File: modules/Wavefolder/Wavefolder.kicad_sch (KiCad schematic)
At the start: 16 parts, among them J10 Conn_Front, J104 WQP-PJ398, J105 WQP-PJ398, J106 WQP-PJ398, J107 WQP-PJ398, J11 Conn_Back, J9 Conn_Eurorack_10, U3 TL072

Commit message: Munger re-design - schematic done, PCB started
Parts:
- added C1, C2: 680N, -lmp-misc:C_Rect_L7.2mm_W4.5mm_P5.00mm, symbol -lmp:CF
- added C3, C4: 10U, -lmp-misc:C_Radial_D5.0mm_H5.0mm_P2.50mm, symbol -lmp-synth:CNP_10U
- added C3, C4: 100N, -lmp-misc:C_Disc_D5.0mm_W2.5mm_P2.50mm, symbol -lmp:CC_100N
- added Q1, Q4, Q6, Q8: 2N3904, -lmp-misc:TO-92_Inline_Wide, symbol -lmp:Q_NPN_2N3904
- added Q2, Q3, Q5, Q7: 2N3906, -lmp-misc:TO-92_Inline_Wide, symbol -lmp:Q_PNP_2N3906
- added R10, R11, R19, R20, R25, R26, R4, R5: 15K, -lmp-misc:R_Axial_DIN0207_L6.3mm_D2.5mm_P7.62mm_Horizontal, symbol -lmp:R_1%_0W166
- added R12, R21, R27, R6: 10K, -lmp-misc:R_Axial_DIN0207_L6.3mm_D2.5mm_P7.62mm_Horizontal, symbol -lmp:R_1%_0W166
- added R13, R28: 200K, -lmp-misc:R_Axial_DIN0207_L6.3mm_D2.5mm_P7.62mm_Horizontal, symbol -lmp:R_1%_0W166
- added R14, R29: 1K, -lmp-misc:R_Axial_DIN0207_L6.3mm_D2.5mm_P10.16mm_Horizontal, symbol -lmp-synth:R_1K_Output
- added R15, R17, R2, R30: 100K, -lmp-misc:R_Axial_DIN0207_L6.3mm_D2.5mm_P7.62mm_Horizontal, symbol -lmp:R_1%_0W166
- added R16: 499K, -lmp-misc:R_Axial_DIN0207_L6.3mm_D2.5mm_P7.62mm_Horizontal, symbol -lmp:R_1%_0W166
- added R18, R3: 18K, -lmp-misc:R_Axial_DIN0207_L6.3mm_D2.5mm_P7.62mm_Horizontal, symbol -lmp:R_1%_0W166
- added R22, R7: 120K, -lmp-misc:R_Axial_DIN0207_L6.3mm_D2.5mm_P7.62mm_Horizontal, symbol -lmp:R_1%_0W166
- added R23, R8: 27K, -lmp-misc:R_Axial_DIN0207_L6.3mm_D2.5mm_P7.62mm_Horizontal, symbol -lmp:R_1%_0W166
- added R24, R9: 68K, -lmp-misc:R_Axial_DIN0207_L6.3mm_D2.5mm_P7.62mm_Horizontal, symbol -lmp:R_1%_0W166
- added U1: TL074, Package_DIP:DIP-14_W7.62mm, symbol -lmp-opamp:TL074
- added U2: TL072, Package_DIP:DIP-8_W7.62mm, symbol -lmp-opamp:TL072
- J10: footprint Connector_PinSocket_2.54mm:PinSocket_1x18_P2.54mm_Vertical -> Connector_PinSocket_2.54mm:PinSocket_1x09_P2.54mm_Vertical; symbol Connector_Generic:Conn_01x18 -> Connector_Generic:Conn_01x09
- J11: footprint Connector_PinHeader_2.54mm:PinHeader_1x18_P2.54mm_Horizontal -> Connector_PinHeader_2.54mm:PinHeader_1x09_P2.54mm_Horizontal; symbol Connector_Generic:Conn_01x18 -> Connector_Generic:Conn_01x09
- renumbered J104 to J1, J106 to J2, J105 to J3, J107 to J4, RV101 to RV1, RV102 to RV2
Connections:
- net +12V: now also C3.1, R10.1, R19.1, R25.1, R4.1, U1.4 (V+); no longer J10.17 (Pin_17), J11.17 (Pin_17)
- net -12V: now also C4.2, R11.2, R20.2, R26.2, R5.2, U1.11 (V-)
- net GND: now also J10.1 (Pin_1), J10.3 (Pin_3), J10.5 (Pin_5), J10.7 (Pin_7), J10.9 (Pin_9), J11.1 (Pin_1), J11.3 (Pin_3), J11.5 (Pin_5), J11.7 (Pin_7), J11.9 (Pin_9), J2.S, J3.S, J4.S, RV2.1, C3.2, C4.1, R15.2, R17.2, R2.2, R24.2, R30.2, R9.2, U1.12 (+), U1.3 (+), U2.3 (+), U2.5 (+); no longer J10.18 (Pin_18), J11.18 (Pin_18)
- net IN-ATTEN-1: now also J10.2 (Pin_2), J11.2 (Pin_2), U1.5 (+)
- net IN-ATTEN-2: now reaches J10.4 (Pin_4), J11.4 (Pin_4)
- net IN-ATTEN-2: now also RV2.2, U1.10 (+)
- net OUT-1: now reaches J10.6 (Pin_6), J11.6 (Pin_6)
- net OUT-1: now also J2.T, J3.TN, C3.2, R15.1
- net OUT-2: now reaches J10.8 (Pin_8), J11.8 (Pin_8)
- net OUT-2: now also J4.T, C4.2, R30.1
- net at RV2.3: now also R16.2
- net at J3.T: now also R16.1
- new net: Q6.1 (E), R20.1
- new net: C2.1, R22.2, U1.14
- new net: C2.2, R23.1
- new net: R13.2, R14.1, U2.1
- new net: R12.2, R13.1, U2.2 (-)
- new net: Q7.1 (E), R25.2
- new net: Q7.2 (B), Q8.2 (B), R23.2, R24.1
- new net: Q7.3 (C), Q8.3 (C), R27.1
- new net: Q5.2 (B), Q6.2 (B), R18.2, U1.8
- new net: R17.1, R18.1, U1.9 (-)
- new net: Q4.1 (E), R11.1
- new net: Q3.2 (B), Q4.2 (B), R8.2, R9.1
- new net: R2.1, R3.1, U1.6 (-)
- new net: Q1.2 (B), Q2.2 (B), R3.2, U1.7
- new net: C4.1, R29.2
- new net: Q3.1 (E), R10.2
- new net: R21.2, R22.1, U1.13 (-)
- new net: Q5.3 (C), Q6.3 (C), R21.1
- new net: Q2.1 (E), R4.2
- new net: C1.1, R7.2, U1.1
- new net: C1.2, R8.1
- new net: Q1.3 (C), Q2.3 (C), R6.1
- new net: R6.2, R7.1, U1.2 (-)
- new net: Q8.1 (E), R26.1
- new net: Q1.1 (E), R5.1
- new net: Q5.1 (E), R19.2
- new net: R27.2, R28.1, U2.6 (-)
- new net: C3.1, R14.2
- new net: Q3.3 (C), Q4.3 (C), R12.1
- new net: R28.2, R29.1, U2.7
- no-connect marks 0 -> 2
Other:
- note added: "Channel 2"
- note added: "TODO: fields for C1, C2"
- note removed: "TODO: normal this from OUT1"
- moved on the sheet: J1, J2, J3, J4, R1, RV1, RV2, U3C

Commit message: Munger re-design - PCB wip
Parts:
- renumbered Q2 to Q1, Q1 to Q2
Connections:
- net GND: now also U2.3 (+), U2.5 (+); no longer U2.3 (+), U2.5 (+)
- net at R13.2, R14.1: now also U2.7; no longer U2.1
- net at R12.2, R13.1: now also U2.6 (-); no longer U2.2 (-)
- net at R27.2, R28.1: now also U2.2 (-); no longer U2.6 (-)
- net at R28.2, R29.1: now also U2.1; no longer U2.7

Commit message: Munger re-design - PCB wip
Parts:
- R20: footprint -lmp-misc:R_Axial_DIN0207_L6.3mm_D2.5mm_P7.62mm_Horizontal -> -lmp-stripboard:SB_Gen_1

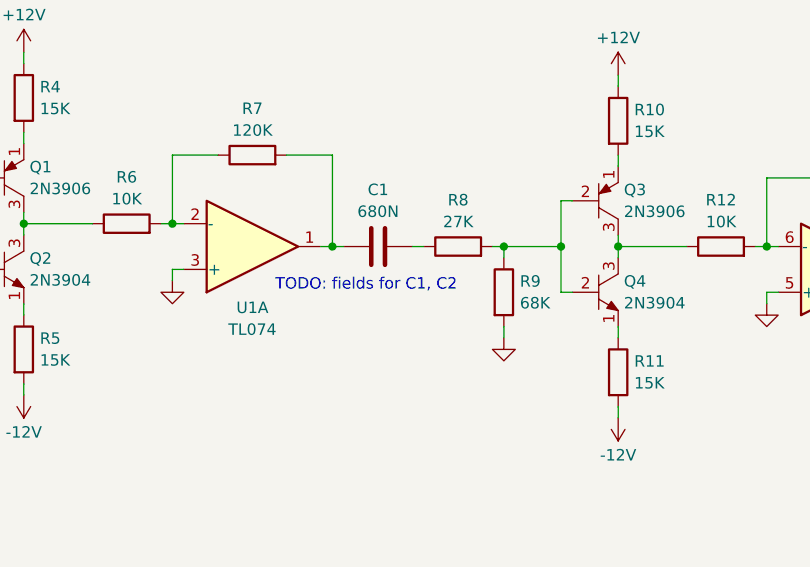
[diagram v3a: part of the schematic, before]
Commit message: Munger re-design - PCB layout mostly done
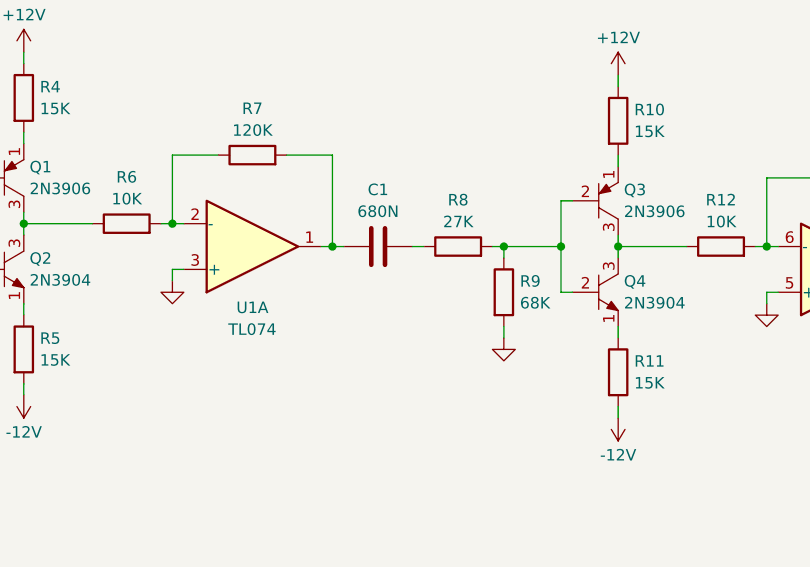
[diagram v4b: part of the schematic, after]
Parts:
- C1, C2: Distributor (none) -> Mouser; DistributorPartLink (none) -> https://www.mouser.ca/ProductDetail/?qs=Jv4FAWB%252B0HZwVuY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; DistributorPartNum (none) -> 80-R82DC3680AA60K; Manufacturer (none) -> KEMET; ManufacturerPartNum (none) -> R82DC3680AA60K
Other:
- note removed: "TODO: fields for C1, C2"

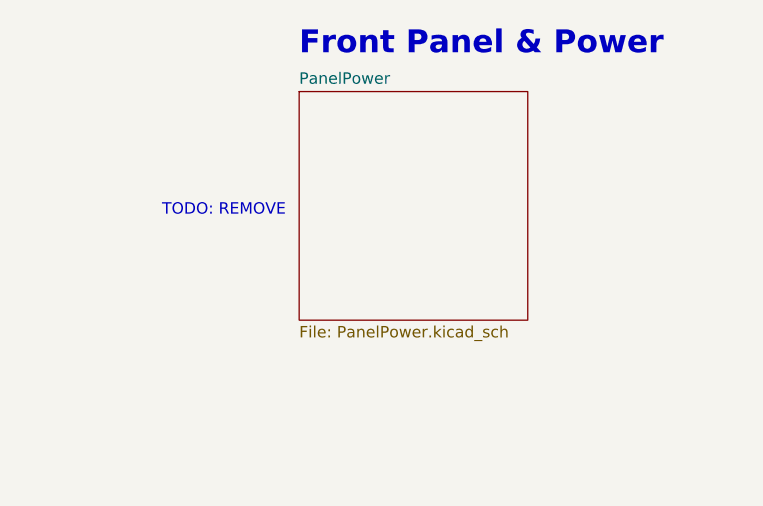
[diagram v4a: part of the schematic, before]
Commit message: Munger re-design - remove unused schematic sheet
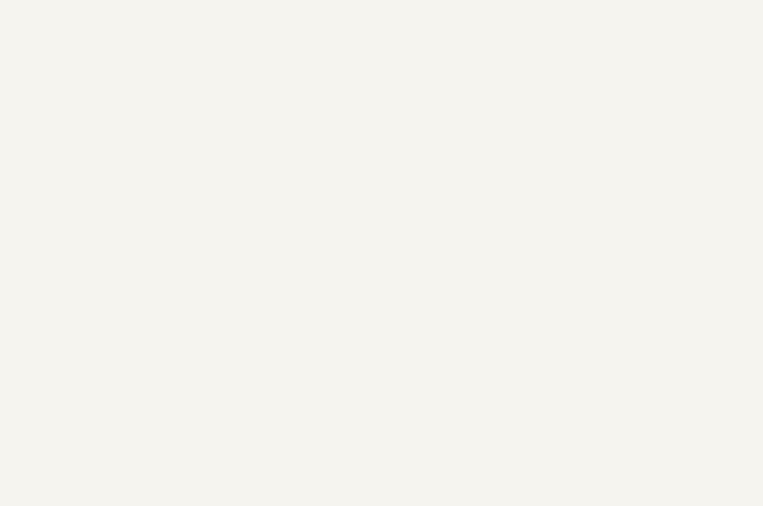
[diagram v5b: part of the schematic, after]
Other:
- removed sheet PanelPower
- note removed: "Front Panel & Power"
- note removed: "TODO: REMOVE"

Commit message: Munger re-design - BOM - wip
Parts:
- C101: renamed from C2; value 10U -> CP_10U
- C102: renamed from C1; value 10U -> CP_10U
- renumbered C3 to C103, C4 to C104, C3 to C105, C4 to C106, J9 to J101, J10 to J102, J11 to J103, U3 to U2

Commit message: Munger re-design - BOM - wip
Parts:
- C101, C102: value CP_10U -> 10U; Value2 35 VDC -> (none)
- R1, R16: DistributorPartLink https://www.mouser.ca/c/?m=YAGEO&power+rating=166+mW+(1%2f6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 -> https://www.mouser.ca/ProductDetail/YAGEO/MFR-25FTE52-499K?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; DistributorPartNum 603-MFR-12* -> 603-MFR-25FTE52-499K; ManufacturerPartNum MFR-12* -> MFR-25FTE52-499K; Value2 1%, 1/6 W -> 1%, 1/4 W
- R10, R11, R19, R20, R25, R26, R4, R5: DistributorPartLink https://www.mouser.ca/c/?m=YAGEO&power+rating=166+mW+(1%2f6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 -> https://www.mouser.ca/ProductDetail/YAGEO/MFR-12FTF52-15K?q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; DistributorPartNum 603-MFR-12* -> 603-MFR-12FTF52-15K; ManufacturerPartNum MFR-12* -> MFR-12FTF52-15K
- R12, R21, R27, R6: DistributorPartLink https://www.mouser.ca/c/?m=YAGEO&power+rating=166+mW+(1%2f6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 -> https://www.mouser.ca/ProductDetail/YAGEO/MFR-12FTF52-10K?q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; DistributorPartNum 603-MFR-12* -> 603-MFR-12FTF52-10K; ManufacturerPartNum MFR-12* -> MFR-12FTF52-10K
- R13, R28: DistributorPartLink https://www.mouser.ca/c/?m=YAGEO&power+rating=166+mW+(1%2f6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 -> https://www.mouser.ca/ProductDetail/YAGEO/MFR-12FTF52-200K?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; DistributorPartNum 603-MFR-12* -> 603-MFR-12FTF52-200K; ManufacturerPartNum MFR-12* -> MFR-12FTF52-200K
- R15, R17, R2, R30: DistributorPartLink https://www.mouser.ca/c/?m=YAGEO&power+rating=166+mW+(1%2f6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 -> https://www.mouser.ca/ProductDetail/YAGEO/MFR-12FTF52-100K?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; DistributorPartNum 603-MFR-12* -> 603-MFR-12FTF52-100K; ManufacturerPartNum MFR-12* -> MFR-12FTF52-100K
- R18, R3: DistributorPartLink https://www.mouser.ca/c/?m=YAGEO&power+rating=166+mW+(1%2f6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 -> https://www.mouser.ca/ProductDetail/YAGEO/MFR-12FTF52-18K?q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; DistributorPartNum 603-MFR-12* -> 603-MFR-12FTF52-18K; ManufacturerPartNum MFR-12* -> MFR-12FTF52-18K
- R22, R7: DistributorPartLink https://www.mouser.ca/c/?m=YAGEO&power+rating=166+mW+(1%2f6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 -> https://www.mouser.ca/ProductDetail/YAGEO/MFR-12FTF52-120K?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; DistributorPartNum 603-MFR-12* -> 603-MFR-12FTF52-120K; ManufacturerPartNum MFR-12* -> MFR-12FTF52-120K
- R23, R8: DistributorPartLink https://www.mouser.ca/c/?m=YAGEO&power+rating=166+mW+(1%2f6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 -> https://www.mouser.ca/ProductDetail/YAGEO/MFR-12FTF52-27K?q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; DistributorPartNum 603-MFR-12* -> 603-MFR-12FTF52-27K; ManufacturerPartNum MFR-12* -> MFR-12FTF52-27K
- R24, R9: DistributorPartLink https://www.mouser.ca/c/?m=YAGEO&power+rating=166+mW+(1%2f6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 -> https://www.mouser.ca/ProductDetail/YAGEO/MFR-12FTF52-68K?q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; DistributorPartNum 603-MFR-12* -> 603-MFR-12FTF52-68K; ManufacturerPartNum MFR-12* -> MFR-12FTF52-68K

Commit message: Munger re-design - fix KiCad project info
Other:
- company: https://lenp.net/synth/ -> Len Popp
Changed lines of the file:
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@@
     (date "2024-04-04")
     (rev "2.0")
-    (company "https://lenp.net/synth/")
-    (comment 1 "Len Popp")
+    (company "Len Popp")
+    (comment 1 "https://lenp.net/synth/")
     (comment 2 "Acknowledgements: Ken Stone; yusynth")
     (comment 3 "Copyright © 2024 Len Popp CC BY")
